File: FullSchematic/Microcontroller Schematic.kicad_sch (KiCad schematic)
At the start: 22 parts, among them J1 USB_B_Micro, U2 CH340C, U3 24LC64, U4 STM32F051C6T6

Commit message: Added uvlo circuit
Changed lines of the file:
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@@
     (stroke (width 0) (type default))
   )
-  (wire (pts (xy 177.673 46.863) (xy 177.673 53.213))
+  (wire (pts (xy 177.673 40.894) (xy 177.673 53.213))
     (stroke (width 0) (type default))
   )
@@
     (effects (font (size 1.27 1.27)) (justify left bottom))
   )
+  (label "5V" (at 177.673 40.894 0) (fields_autoplaced)
+    (effects (font (size 1.27 1.27)) (justify left bottom))
+  )

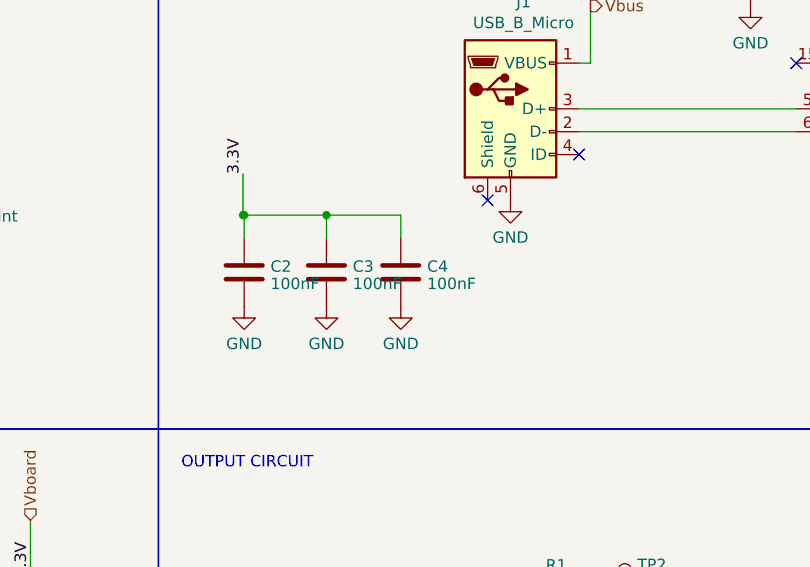
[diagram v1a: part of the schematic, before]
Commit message: updated microcontroller BOM and added qr code to b.silk
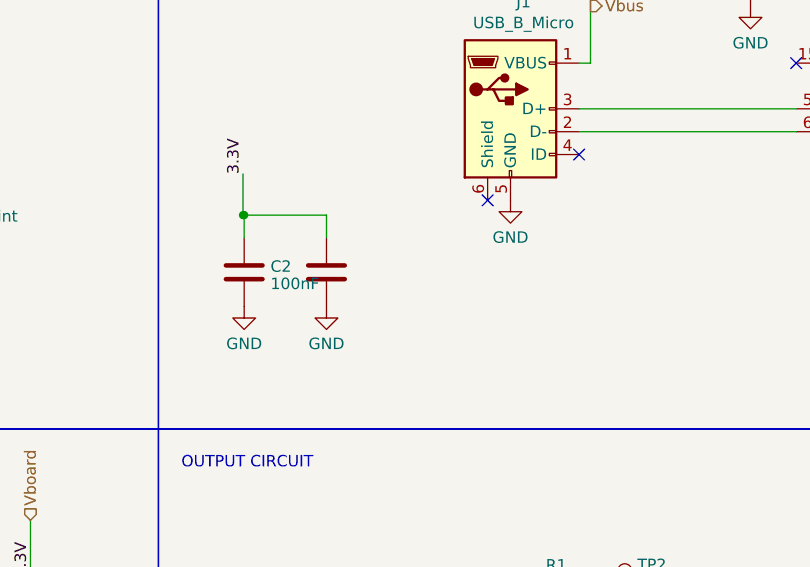
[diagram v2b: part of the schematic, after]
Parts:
- removed C4: 100nF, Library:CAPC1608X90N, symbol Device:C
- C1, C2, C3: Price 0.08 -> $0.0138; Price ( 1 board) 0.32 -> 0.0414; Price (5 boards) 1.6 -> 0.069
- D1, D2, D3: JLCPCB Part # N/A -> C54142; Price (5 boards) 0.2085 -> 0.0695
- J1: Price $0.0273 -> $0.0333; Price ( 1 board) 0.0273 -> $0.0333; Price (5 boards) 0.1365 -> $0.1665
- R6: Price $0.0005 -> 0.001
- U3: Price $0.5172 -> $0.7664; Price ( 1 board) 0.5172 -> $0.7664; Price (5 boards) 2.586 -> 3.832
- U4: JLCPCB Part # N/A -> C5456
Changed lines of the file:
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@@
   (junction (at 208.153 36.703) (diameter 0) (color 0 0 0 0)
-  )
-  (junction (at 148.336 70.104) (diameter 0) (color 0 0 0 0)
   )
   (junction (at 139.065 70.104) (diameter 0) (color 0 0 0 0)
@@
     (stroke (width 0) (type default))
   )
-  (wire (pts (xy 156.591 70.104) (xy 156.591 72.644))
-    (stroke (width 0) (type default))
-  )
   (wire (pts (xy 87.249 46.101) (xy 87.249 51.181))
-    (stroke (width 0) (type default))
-  )
-  (wire (pts (xy 148.336 70.104) (xy 156.591 70.104))
     (stroke (width 0) (type default))
   )
@@
       (effects (font (size 1.27 1.27)) hide)
     )
-    (property "Price (5 boards)" "0.2085" (at 194.183 130.683 0)
-      (effects (font (size 1.27 1.27)) hide)
-    )
-    (property "JLCPCB Part #" "N/A" (at 194.183 130.683 0)
+    (property "Price (5 boards)" "0.0695" (at 194.183 130.683 0)
+      (effects (font (size 1.27 1.27)) hide)
+    )
+    (property "JLCPCB Part #" "C54142" (at 194.183 130.683 0)
       (effects (font (size 1.27 1.27)) hide)
     )
@@
       (effects (font (size 1.27 1.27)) hide)
     )
-    (property "Price (5 boards)" "0.2085" (at 194.183 121.793 0)
-      (effects (font (size 1.27 1.27)) hide)
-    )
-    (property "JLCPCB Part #" "N/A" (at 194.183 121.793 0)
+    (property "Price (5 boards)" "0.0695" (at 194.183 121.793 0)
+      (effects (font (size 1.27 1.27)) hide)
+    )
+    (property "JLCPCB Part #" "C54142" (at 194.183 121.793 0)
       (effects (font (size 1.27 1.27)) hide)
     )
@@
       (effects (font (size 1.27 1.27)) hide)
     )
-    (property "Price (5 boards)" "0.2085" (at 194.183 112.903 0)
-      (effects (font (size 1.27 1.27)) hide)
-    )
-    (property "JLCPCB Part #" "N/A" (at 194.183 112.903 0)
+    (property "Price (5 boards)" "0.0695" (at 194.183 112.903 0)
+      (effects (font (size 1.27 1.27)) hide)
+    )
+    (property "JLCPCB Part #" "C54142" (at 194.183 112.903 0)
       (effects (font (size 1.27 1.27)) hide)
     )
@@
       (effects (font (size 1.27 1.27)) hide)
     )
-    (property "Price" "$0.0273" (at 168.783 58.293 0)
-      (effects (font (size 1.27 1.27)) hide)
-    )
-    (property "Price ( 1 board)" "0.0273" (at 168.783 58.293 0)
-      (effects (font (size 1.27 1.27)) hide)
-    )
-    (property "Price (5 boards)" "0.1365" (at 168.783 58.293 0)
+    (property "Price" "$0.0333" (at 168.783 58.293 0)
+      (effects (font (size 1.27 1.27)) hide)
+    )
+    (property "Price ( 1 board)" "$0.0333" (at 168.783 58.293 0)
+      (effects (font (size 1.27 1.27)) hide)
+    )
+    (property "Price (5 boards)" "$0.1665" (at 168.783 58.293 0)
       (effects (font (size 1.27 1.27)) hide)
     )
@@
       (effects (font (size 1.27 1.27)) hide)
     )
-    (property "Price" "0.08" (at 195.453 43.053 0)
-      (effects (font (size 1.27 1.27)) hide)
-    )
-    (property "Price ( 1 board)" "0.32" (at 195.453 43.053 0)
-      (effects (font (size 1.27 1.27)) hide)
-    )
-    (property "Price (5 boards)" "1.6" (at 195.453 43.053 0)
+    (property "Price" " $0.0138" (at 195.453 43.053 0)
+      (effects (font (size 1.27 1.27)) hide)
+    )
+    (property "Price ( 1 board)" "0.0414" (at 195.453 43.053 0)
+      (effects (font (size 1.27 1.27)) hide)
+    )
+    (property "Price (5 boards)" "0.069" (at 195.453 43.053 0)
       (effects (font (size 1.27 1.27)) hide)
     )
@@
       (effects (font (size 1.27 1.27)) hide)
     )
-    (property "Price" "$0.5172" (at 87.249 61.341 0)
-      (effects (font (size 1.27 1.27)) hide)
-    )
-    (property "Price ( 1 board)" "0.5172" (at 87.249 61.341 0)
-      (effects (font (size 1.27 1.27)) hide)
-    )
-    (property "Price (5 boards)" "2.586" (at 87.249 61.341 0)
+    (property "Price" "$0.7664" (at 87.249 61.341 0)
+      (effects (font (size 1.27 1.27)) hide)
+    )
+    (property "Price ( 1 board)" "$0.7664" (at 87.249 61.341 0)
+      (effects (font (size 1.27 1.27)) hide)
+    )
+    (property "Price (5 boards)" "3.832" (at 87.249 61.341 0)
       (effects (font (size 1.27 1.27)) hide)
     )
@@
     (in_bom yes) (on_board yes) (dnp no) (fields_autoplaced)
     (property "Reference" "C3" (at 151.257 75.8103 0)
-      (effects (font (size 1.27 1.27)) (justify left))
+      (effects (font (size 1.27 1.27)) (justify left) hide)
     )
     (property "Value" "100nF" (at 151.257 77.7313 0)
-      (effects (font (size 1.27 1.27)) (justify left))
+      (effects (font (size 1.27 1.27)) (justify left) hide)
     )
     (property "Footprint" "Library:CAPC1608X90N" (at 149.3012 80.264 0)
@@
       (effects (font (size 1.27 1.27)) hide)
     )
-    (property "Price" "0.08" (at 148.336 76.454 0)
-      (effects (font (size 1.27 1.27)) hide)
-    )
-    (property "Price ( 1 board)" "0.32" (at 148.336 76.454 0)
-      (effects (font (size 1.27 1.27)) hide)
-    )
-    (property "Price (5 boards)" "1.6" (at 148.336 76.454 0)
+    (property "Price" " $0.0138" (at 148.336 76.454 0)
+      (effects (font (size 1.27 1.27)) hide)
+    )
+    (property "Price ( 1 board)" "0.0414" (at 148.336 76.454 0)
+      (effects (font (size 1.27 1.27)) hide)
+    )
+    (property "Price (5 boards)" "0.069" (at 148.336 76.454 0)
       (effects (font (size 1.27 1.27)) hide)
     )
@@
       (effects (font (size 1.27 1.27)) hide)
     )
-    (property "Price" "0.08" (at 139.192 76.454 0)
-      (effects (font (size 1.27 1.27)) hide)
-    )
-    (property "Price ( 1 board)" "0.32" (at 139.192 76.454 0)
-      (effects (font (size 1.27 1.27)) hide)
-    )
-    (property "Price (5 boards)" "1.6" (at 139.192 76.454 0)
+    (property "Price" " $0.0138" (at 139.192 76.454 0)
+      (effects (font (size 1.27 1.27)) hide)
+    )
+    (property "Price ( 1 board)" "0.0414" (at 139.192 76.454 0)
+      (effects (font (size 1.27 1.27)) hide)
+    )
+    (property "Price (5 boards)" "0.069" (at 139.192 76.454 0)
       (effects (font (size 1.27 1.27)) hide)
     )
@@
         (path "/5dd86611-a33d-45ee-946c-01c599f30b12/5d08bf44-0550-4275-b6e8-e4566a125a74"
           (reference "#PWR013") (unit 1)
-        )
-      )
-      (project "Microcontroller Schematic"
-        (path "/87ad8a26-ca2b-40e6-a130-1e9e8587d367"
-          (reference "#PWR03") (unit 1)
-        )
-      )
-    )
-  )
-  (symbol (lib_id "power:GND") (at 156.591 80.264 0) (unit 1)
-    (in_bom yes) (on_board yes) (dnp no) (fields_autoplaced)
-    (property "Reference" "#PWR014" (at 156.591 86.614 0)
-      (effects (font (size 1.27 1.27)) hide)
-    )
-    (property "Value" "GND" (at 156.591 84.3995 0)
-      (effects (font (size 1.27 1.27)))
-    )
-    (property "Footprint" "" (at 156.591 80.264 0)
-      (effects (font (size 1.27 1.27)) hide)
-    )
-    (property "Datasheet" "" (at 156.591 80.264 0)
-      (effects (font (size 1.27 1.27)) hide)
-    )
-    (pin "1")
-    (instances
-      (project "FullSchematic"
-        (path "/5dd86611-a33d-45ee-946c-01c599f30b12/5d08bf44-0550-4275-b6e8-e4566a125a74"
-          (reference "#PWR014") (unit 1)
         )
       )
@@
       (effects (font (size 1.27 1.27)) hide)
     )
-    (property "Price" "$0.0005 " (at 93.599 46.101 0)
+    (property "Price" "0.001" (at 93.599 46.101 0)
       (effects (font (size 1.27 1.27)) hide)
     )
@@
     )
   )
-  (symbol (lib_id "Device:C") (at 156.591 76.454 0) (unit 1)
-    (in_bom yes) (on_board yes) (dnp no) (fields_autoplaced)
-    (property "Reference" "C4" (at 159.512 75.8103 0)
-      (effects (font (size 1.27 1.27)) (justify left))
-    )
-    (property "Value" "100nF" (at 159.512 77.7313 0)
-      (effects (font (size 1.27 1.27)) (justify left))
-    )
-    (property "Footprint" "Library:CAPC1608X90N" (at 157.5562 80.264 0)
-      (effects (font (size 1.27 1.27)) hide)
-    )
-    (property "Datasheet" "~" (at 156.591 76.454 0)
-      (effects (font (size 1.27 1.27)) hide)
-    )
-    (property "Price" "0.08" (at 156.591 76.454 0)
-      (effects (font (size 1.27 1.27)) hide)
-    )
-    (property "Price ( 1 board)" "0.32" (at 156.591 76.454 0)
-      (effects (font (size 1.27 1.27)) hide)
-    )
-    (property "Price (5 boards)" "1.6" (at 156.591 76.454 0)
-      (effects (font (size 1.27 1.27)) hide)
-    )
-    (property "JLCPCB Part #" "C24497" (at 156.591 76.454 0)
-      (effects (font (size 1.27 1.27)) hide)
-    )
-    (pin "1")
-    (pin "2")
-    (instances
-      (project "FullSchematic"
-        (path "/5dd86611-a33d-45ee-946c-01c599f30b12/5d08bf44-0550-4275-b6e8-e4566a125a74"
-          (reference "C4") (unit 1)
-        )
-      )
-      (project "Microcontroller Schematic"
-        (path "/87ad8a26-ca2b-40e6-a130-1e9e8587d367"
-          (reference "C7") (unit 1)
-        )
-      )
-    )
-  )
   (symbol (lib_id "power:GND") (at 210.693 76.073 0) (unit 1)
     (in_bom yes) (on_board yes) (dnp no) (fields_autoplaced)
@@
       (effects (font (size 1.27 1.27)) hide)
     )
-    (property "JLCPCB Part #" "N/A" (at 93.853 135.763 0)
-      (effects (font (size 1.27 1.27)) hide)
-    )
+    (property "JLCPCB Part #" "C5456" (at 93.853 135.763 0)
+      (effects (font (size 1.27 1.27)) hide)
+    )

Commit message: Confirmed part numbers and prices
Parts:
- added C4: 100nF, Capacitor_SMD:C_1206_3216Metric, symbol Device:C
- added J4: Conn_01x03_Pin, Connector_PinHeader_2.54mm:PinHeader_1x03_P2.54mm_Vertical, symbol Connector:Conn_01x03_Pin
- C1, C2, C3: footprint Library:CAPC1608X90N -> Capacitor_SMD:C_1206_3216Metric; Populate (none) -> Yes
- D1, D2, D3, J1, R6, U2, U3: Populate (none) -> Yes
- R1, R2, R3: value 270 -> 270R; footprint Library:RESC2013X65N -> Resistor_SMD:R_1206_3216Metric; Populate (none) -> Yes
- TP17: footprint TestPoint:TestPoint_Loop_D3.80mm_Drill2.0mm -> TestPoint:TestPoint_Keystone_5005-5009_Compact
- U4: Populate (none) -> No
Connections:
- net GND: now also C4.2
- net Vboard: now also C4.1, J4.1 (Pin_1); no longer C1.1, U2.16 (VCC), U2.4 (V3)
- net Vbus: now also J4.3 (Pin_3)
- new net: C1.1, J4.2 (Pin_2), U2.16 (VCC), U2.4 (V3)

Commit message: generated files
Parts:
- J4, TP1, TP17, TP2, TP3, TP4, TP6, TP7: JLCPCB Part # N/A -> (none)
- U4: JLCPCB Part # C5456 -> (none)
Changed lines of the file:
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@@
       (effects (font (size 1.27 1.27)) hide)
     )
-    (property "JLCPCB Part #" "N/A" (at 80.899 51.181 0)
+    (property "JLCPCB Part #" "" (at 80.899 51.181 0)
       (effects (font (size 1.27 1.27)) hide)
     )
@@
       (effects (font (size 1.27 1.27)) hide)
     )
-    (property "JLCPCB Part #" "N/A" (at 180.213 130.683 0)
+    (property "JLCPCB Part #" "" (at 180.213 130.683 0)
       (effects (font (size 1.27 1.27)) hide)
     )
@@
       (effects (font (size 1.27 1.27)) hide)
     )
-    (property "JLCPCB Part #" "N/A" (at 181.483 112.903 0)
+    (property "JLCPCB Part #" "" (at 181.483 112.903 0)
       (effects (font (size 1.27 1.27)) hide)
     )
@@
       (effects (font (size 1.27 1.27)) hide)
     )
-    (property "JLCPCB Part #" "N/A" (at 175.26 31.242 0)
+    (property "JLCPCB Part #" "" (at 175.26 31.242 0)
       (effects (font (size 1.27 1.27)) hide)
     )
@@
       (effects (font (size 1.27 1.27)) hide)
     )
-    (property "JLCPCB Part #" "N/A" (at 88.138 100.457 0)
+    (property "JLCPCB Part #" "" (at 88.138 100.457 0)
       (effects (font (size 1.27 1.27)) hide)
     )
@@
       (effects (font (size 1.27 1.27)) hide)
     )
-    (property "JLCPCB Part #" "N/A" (at 72.009 161.163 0)
+    (property "JLCPCB Part #" "" (at 72.009 161.163 0)
       (effects (font (size 1.27 1.27)) hide)
     )
@@
       (effects (font (size 1.27 1.27)) hide)
     )
-    (property "JLCPCB Part #" "N/A" (at 181.483 121.793 0)
+    (property "JLCPCB Part #" "" (at 181.483 121.793 0)
       (effects (font (size 1.27 1.27)) hide)
     )
@@
       (effects (font (size 1.27 1.27)) hide)
     )
-    (property "JLCPCB Part #" "N/A" (at 101.219 68.961 0)
+    (property "JLCPCB Part #" "" (at 101.219 68.961 0)
       (effects (font (size 1.27 1.27)) hide)
     )
@@
       (effects (font (size 1.27 1.27)) hide)
     )
-    (property "JLCPCB Part #" "C5456" (at 93.853 135.763 0)
-      (effects (font (size 1.27 1.27)) hide)
-    )
+    (property "JLCPCB Part #" "" (at 93.853 135.763 0)
+      (effects (font (size 1.27 1.27)) hide)
+    )

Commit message: Decreased Price
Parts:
- R1, R2, R3: footprint Resistor_SMD:R_1206_3216Metric -> Resistor_SMD:R_0805_2012Metric; JLCPCB Part # C4466 -> C17590
- U3: value 24LC64 -> AT24C256C; JLCPCB Part # C511260 -> C6482
- U4: now not fitted; now left out of the parts list
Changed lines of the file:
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@@
       (effects (font (size 1.27 1.27)))
     )
-    (property "Footprint" "Resistor_SMD:R_1206_3216Metric" (at 174.117 111.887 90)
+    (property "Footprint" "Resistor_SMD:R_0805_2012Metric" (at 174.117 111.887 90)
       (effects (font (size 1.27 1.27)) hide)
     )
@@
       (effects (font (size 1.27 1.27)) hide)
     )
-    (property "JLCPCB Part #" "C4466" (at 173.863 112.903 0)
+    (property "JLCPCB Part #" "C17590" (at 173.863 112.903 0)
       (effects (font (size 1.27 1.27)) hide)
     )
@@
       (effects (font (size 1.27 1.27)))
     )
-    (property "Footprint" "Resistor_SMD:R_1206_3216Metric" (at 174.117 129.667 90)
+    (property "Footprint" "Resistor_SMD:R_0805_2012Metric" (at 174.117 129.667 90)
       (effects (font (size 1.27 1.27)) hide)
     )
@@
       (effects (font (size 1.27 1.27)) hide)
     )
-    (property "JLCPCB Part #" "C4466" (at 173.863 130.683 0)
+    (property "JLCPCB Part #" "C17590" (at 173.863 130.683 0)
       (effects (font (size 1.27 1.27)) hide)
     )
@@
       (effects (font (size 1.27 1.27)) (justify left))
     )
-    (property "Value" "24LC64" (at 89.2049 55.1721 0)
+    (property "Value" "AT24C256C" (at 89.2049 55.1721 0)
       (effects (font (size 1.27 1.27)) (justify left))
     )
@@
       (effects (font (size 1.27 1.27)) hide)
     )
-    (property "JLCPCB Part #" "C511260" (at 87.249 61.341 0)
+    (property "JLCPCB Part #" "C6482" (at 87.249 61.341 0)
       (effects (font (size 1.27 1.27)) hide)
     )
@@
       (effects (font (size 1.27 1.27)))
     )
-    (property "Footprint" "Resistor_SMD:R_1206_3216Metric" (at 174.117 120.777 90)
+    (property "Footprint" "Resistor_SMD:R_0805_2012Metric" (at 174.117 120.777 90)
       (effects (font (size 1.27 1.27)) hide)
     )
@@
       (effects (font (size 1.27 1.27)) hide)
     )
-    (property "JLCPCB Part #" "C4466" (at 173.863 121.793 0)
+    (property "JLCPCB Part #" "C17590" (at 173.863 121.793 0)
       (effects (font (size 1.27 1.27)) hide)
     )
@@
   )
   (symbol (lib_id "UCT:STM32F051C6TG6_Target") (at 93.853 135.763 0) (unit 1)
-    (in_bom yes) (on_board yes) (dnp no) (fields_autoplaced)
+    (in_bom no) (on_board yes) (dnp yes) (fields_autoplaced)
     (property "Reference" "U4" (at 98.9839 171.323 0)
       (effects (font (size 1.27 1.27)) (justify left))
